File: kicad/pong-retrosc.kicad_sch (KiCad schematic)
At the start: 26 parts, among them J1 RCA video (painel), J10 PAM8403 OUT L (painel), J2 PAM8403 IN, J3 PAM8403 5V, J4 chave A/B (linha), J5 pot P1 (painel), J6 pot P2 (painel), J7 START (painel), J8 RCA audio L (painel), J9 RCA audio R (painel), SW1 START, SW2 A/B, U1 RaspberryPi_Pico

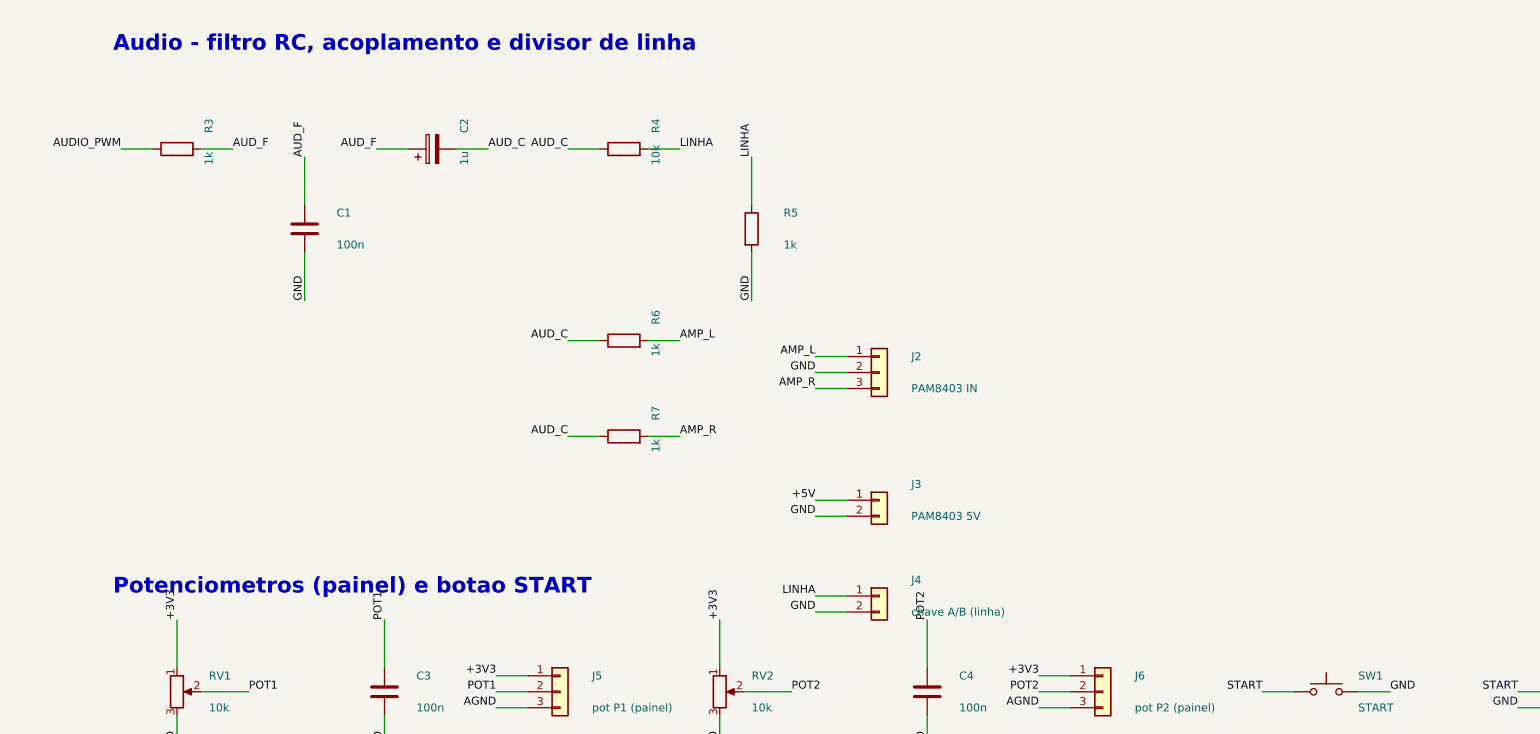
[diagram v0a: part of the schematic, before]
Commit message: kicad: sobe o ramo do amp e afasta titulo dos labels dos pots
Move R6/R7/J2/J3/J4 para a faixa do audio, a direita (antes desciam
ate U(64) e o J4 batia na linha do titulo dos potenciometros).

Sobe o titulo "Potenciometros" para U(58): os labels +3V3/POT1/POT2
sobem dos pots e alcancavam ~U(65), colidindo com o texto.

ERC continua com 0 violacoes; SVG e PDF regerados.

Co-Authored-By: Claude Opus 4.7 <noreply@anthropic.com>
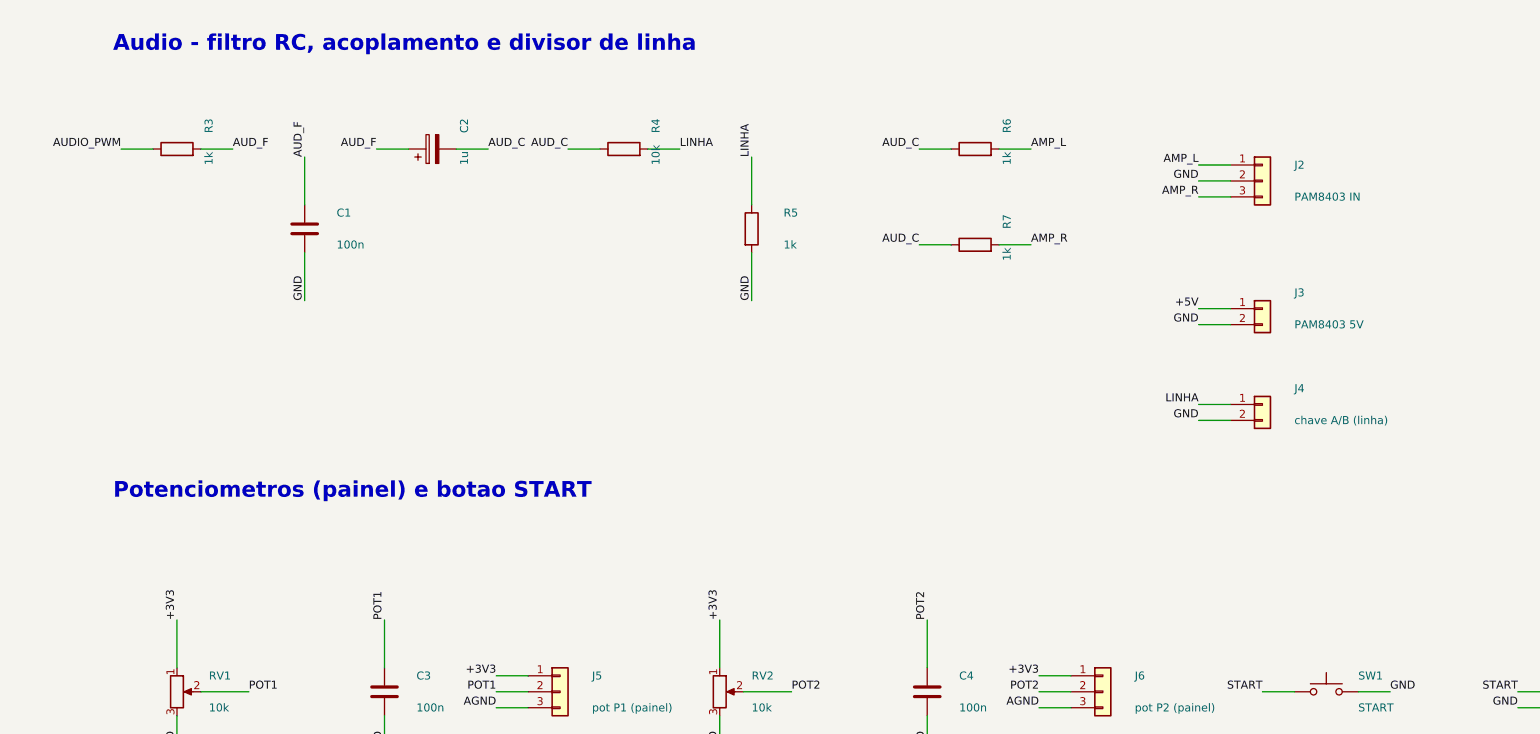
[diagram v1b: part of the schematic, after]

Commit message: kicad: esquematico refeito para a arquitetura do prototipo
As fotos do prototipo mostram RCAs e o modulo PAM8403 soldados NA
PLACA -- o esquematico tratava os dois como pecas de painel. Corrige:

- J1/J8/J9 (RCAs de video e audio) e U2 (PAM8403 HW-012) passam a ser
  on-board, com footprint.
- Substitui os headers J2/J3 (entradas/5V do amp) pelo proprio modulo
  U2, com Rout+/Rout- em No-Connect (audio e mono).
- A chave A/B fica no painel e chega por J4, agora header de 6 vias
  (RCA_C, RCA_S, LINHA, GND, LOUT_P, LOUT_N). Remove J10.
- Off-board seguem apenas: pots (J5/J6), START (J7) e a chave (J4).

Novo tools/gen_kicad_fp.py cria os dois footprints que nao existem nas
libs do KiCad (jack RCA e modulo PAM8403); validados com
"kicad-cli fp export svg". Registra a lib do projeto em fp-lib-table.

ATENCAO: as medidas desses dois footprints ainda sao PROVISORIAS --
estao marcadas com [MEDIR] no gerador e precisam ser conferidas contra
as pecas reais antes de fabricar.

ERC continua em 0 violacoes.

Co-Authored-By: Claude Opus 4.7 <noreply@anthropic.com>
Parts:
- removed J10: PAM8403 OUT L (painel), symbol Connector_Generic:Conn_01x02
- removed J2: PAM8403 IN, Connector_PinHeader_2.54mm:PinHeader_1x03_P2.54mm_Vertical, symbol Connector_Generic:Conn_01x03
- removed J3: PAM8403 5V, Connector_PinHeader_2.54mm:PinHeader_1x02_P2.54mm_Vertical, symbol Connector_Generic:Conn_01x02
- removed J4: chave A/B (linha), Connector_PinHeader_2.54mm:PinHeader_1x02_P2.54mm_Vertical, symbol Connector_Generic:Conn_01x02
- added J4: chave A/B (painel), Connector_PinHeader_2.54mm:PinHeader_1x06_P2.54mm_Vertical, symbol Connector_Generic:Conn_01x06
- added U2: PAM8403 HW-012, pong-retrosc:PAM8403_HW-012, symbol Connector_Generic:Conn_01x08
- J1: value RCA video (painel) -> RCA video (na placa); footprint Connector_PinHeader_2.54mm:PinHeader_1x02_P2.54mm_Vertical -> pong-retrosc:RCA_Jack_THT_Panel
- J8: value RCA audio L (painel) -> RCA audio L (na placa); footprint (none) -> pong-retrosc:RCA_Jack_THT_Panel
- J9: value RCA audio R (painel) -> RCA audio R (na placa); footprint (none) -> pong-retrosc:RCA_Jack_THT_Panel
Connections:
- net +5V: now also U2.1 (Pin_1)
- net AMP_L: now also U2.3 (Pin_3)
- net AMP_R: now also U2.4 (Pin_4)
- net GND: now also J4.4 (Pin_4), U2.2 (Pin_2)
- net LINHA: now also J4.3 (Pin_3)
- net LOUT_N: now also J4.6 (Pin_6), U2.6 (Pin_6)
- net LOUT_P: now also J4.5 (Pin_5), U2.5 (Pin_5)
- net RCA_C: now also J4.1 (Pin_1)
- net RCA_S: now also J4.2 (Pin_2)
- no-connect marks 24 -> 26
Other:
- note added: "Chave A/B (painel, via J4) e RCAs de audio (na placa)"
- note removed: "Chave A/B e RCAs de audio - PAINEL (fora da placa)"

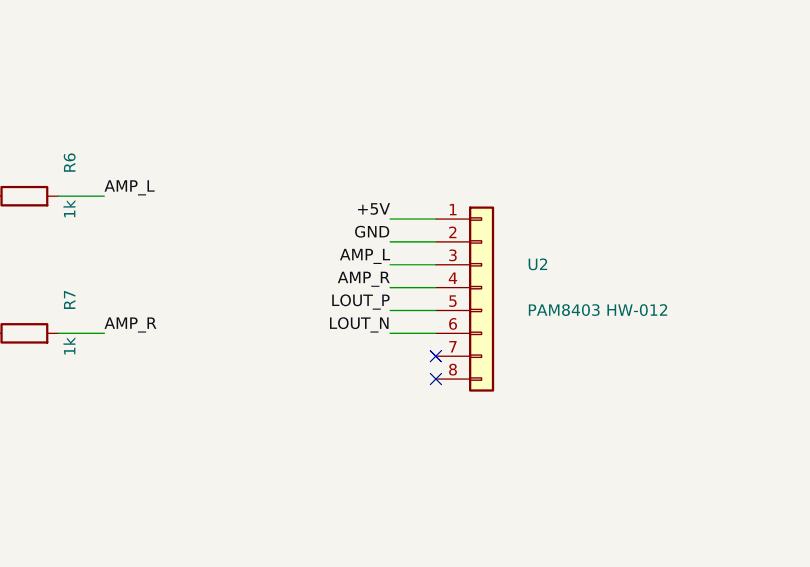
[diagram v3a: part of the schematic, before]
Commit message: kicad: PCB roteado (2 camadas, plano de GND, DRC 0 erros)
Placa gerada e roteada por scripts, reproduzivel:
- tools/gen_kicad_pcb.py: placement (audio a esquerda, video a direita
  com retornos separados; Pico no meio; headers de painel na frente),
  contorno 100x60, furos M3, zonas GND nas 2 faces e regras JLCPCB.
- tools/make_decoy.py: placa-isca sem zonas + contorno recuado 0.35mm,
  para o Freerouting rotear nas 2 camadas (com zonas ele vira quase
  mono-camada e abandona nets longos -- licao da skill kicad-freerouting).
- tools/import_ses.py: importa o SES e remove as trilhas de GND (o plano
  cuida do GND via thermal), eliminando o starved_thermal.

Freerouting roteou os 36 nets; DRC final (--refill-zones) com 0 erros
eletricos (0 unconnected/clearance/shorting/edge). Restam so avisos de
silk (cosmeticos).

Corrige a pinagem do U2 (Conn_01x09 na ordem fisica do HW-012) e ajusta
os footprints do RCA (medidas reais: sinal + 3 abas de terra a 5mm,
furos oblongos) e do PAM8403 (montagem vertical/SIP).

Inclui gerbers + furacao em kicad/gerbers/ e kicad/README.md com o
pipeline completo. Remove tools/post_route.py (obsoleto: era o
roteamento manual dos 2 nets que a isca resolveu).

Co-Authored-By: Claude Opus 4.7 <noreply@anthropic.com>
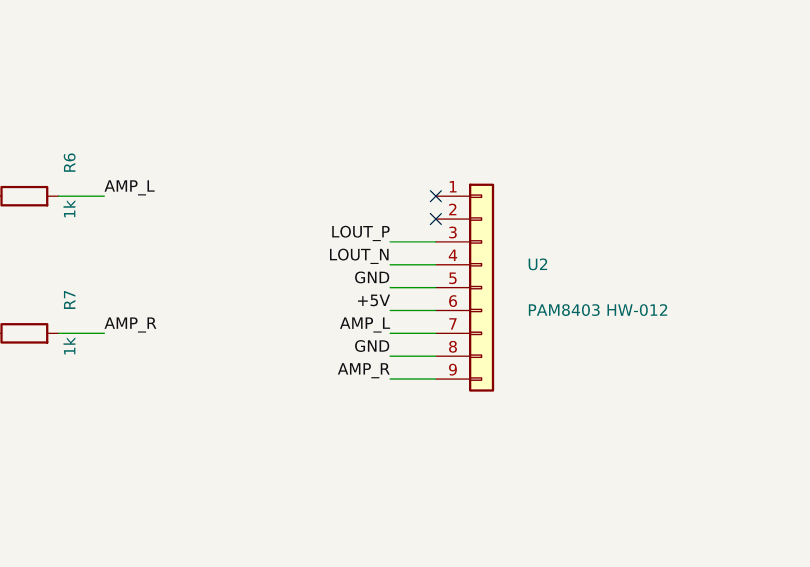
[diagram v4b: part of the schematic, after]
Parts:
- removed U2: PAM8403 HW-012, pong-retrosc:PAM8403_HW-012, symbol Connector_Generic:Conn_01x08
- added U2: PAM8403 HW-012, pong-retrosc:PAM8403_HW-012, symbol Connector_Generic:Conn_01x09
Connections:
- net +5V: now also U2.6 (Pin_6)
- net AMP_L: now also U2.7 (Pin_7)
- net AMP_R: now also U2.9 (Pin_9)
- net GND: now also U2.5 (Pin_5), U2.8 (Pin_8)
- net LOUT_N: now also U2.4 (Pin_4)
- net LOUT_P: now also U2.3 (Pin_3)
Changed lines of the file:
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@@
 		(instances
 			(project "pong-retrosc"
-				(path "/96b8633d-64ce-4605-8e3d-9ed899d2ea24"
+				(path "/54382c2c-30b3-43b0-8332-7c9095b4b1c1"
 					(reference "U1")
 					(unit 1)
@@
 		(instances
 			(project "pong-retrosc"
-				(path "/96b8633d-64ce-4605-8e3d-9ed899d2ea24"
+				(path "/54382c2c-30b3-43b0-8332-7c9095b4b1c1"
 					(reference "R1")
 					(unit 1)
@@
 		(instances
 			(project "pong-retrosc"
-				(path "/96b8633d-64ce-4605-8e3d-9ed899d2ea24"
+				(path "/54382c2c-30b3-43b0-8332-7c9095b4b1c1"
 					(reference "R2")
 					(unit 1)
@@
 		(instances
 			(project "pong-retrosc"
-				(path "/96b8633d-64ce-4605-8e3d-9ed899d2ea24"
+				(path "/54382c2c-30b3-43b0-8332-7c9095b4b1c1"
 					(reference "J1")
 					(unit 1)
@@
 		(instances
 			(project "pong-retrosc"
-				(path "/96b8633d-64ce-4605-8e3d-9ed899d2ea24"
+				(path "/54382c2c-30b3-43b0-8332-7c9095b4b1c1"
 					(reference "R3")
 					(unit 1)
@@
 		(instances
 			(project "pong-retrosc"
-				(path "/96b8633d-64ce-4605-8e3d-9ed899d2ea24"
+				(path "/54382c2c-30b3-43b0-8332-7c9095b4b1c1"
 					(reference "C1")
 					(unit 1)
@@
 		(instances
 			(project "pong-retrosc"
-				(path "/96b8633d-64ce-4605-8e3d-9ed899d2ea24"
+				(path "/54382c2c-30b3-43b0-8332-7c9095b4b1c1"
 					(reference "C2")
 					(unit 1)
@@
 		(instances
 			(project "pong-retrosc"
-				(path "/96b8633d-64ce-4605-8e3d-9ed899d2ea24"
+				(path "/54382c2c-30b3-43b0-8332-7c9095b4b1c1"
 					(reference "R4")
 					(unit 1)
@@
 		(instances
 			(project "pong-retrosc"
-				(path "/96b8633d-64ce-4605-8e3d-9ed899d2ea24"
+				(path "/54382c2c-30b3-43b0-8332-7c9095b4b1c1"
 					(reference "R5")
 					(unit 1)
@@
 		(instances
 			(project "pong-retrosc"
-				(path "/96b8633d-64ce-4605-8e3d-9ed899d2ea24"
+				(path "/54382c2c-30b3-43b0-8332-7c9095b4b1c1"
 					(reference "R6")
 					(unit 1)
@@
 		(instances
 			(project "pong-retrosc"
-				(path "/96b8633d-64ce-4605-8e3d-9ed899d2ea24"
+				(path "/54382c2c-30b3-43b0-8332-7c9095b4b1c1"
 					(reference "R7")
 					(unit 1)
@@
 	)
 	(symbol
-		(lib_id "Connector_Generic:Conn_01x08")
+		(lib_id "Connector_Generic:Conn_01x09")
 		(at 309.88 101.6 0)
 		(unit 1)
@@
 		(pin "7")
 		(pin "8")
+		(pin "9")
 		(instances
 			(project "pong-retrosc"
-				(path "/96b8633d-64ce-4605-8e3d-9ed899d2ea24"
+				(path "/54382c2c-30b3-43b0-8332-7c9095b4b1c1"
 					(reference "U2")
 					(unit 1)
@@
 	(wire
 		(pts
-			(xy 304.8 93.98) (xy 299.72 93.98)
+			(xy 304.8 96.52) (xy 299.72 96.52)
 		)
 		(stroke
@@
 		)
 	)
-	(label "+5V"
-		(at 299.72 93.98 0)
+	(label "LOUT_P"
+		(at 299.72 96.52 0)
 		(effects
 			(font
@@
 	(wire
 		(pts
-			(xy 304.8 96.52) (xy 299.72 96.52)
+			(xy 304.8 99.06) (xy 299.72 99.06)
+		)
+		(stroke
+			(width 0)
+			(type default)
+		)
+	)
+	(label "LOUT_N"
+		(at 299.72 99.06 0)
+		(effects
+			(font
+				(size 1.27 1.27)
+			)
+			(justify right bottom)
+		)
+	)
+	(wire
+		(pts
+			(xy 304.8 101.6) (xy 299.72 101.6)
 		)
 		(stroke
@@
 	)
 	(label "GND"
-		(at 299.72 96.52 0)
+		(at 299.72 101.6 0)
 		(effects
 			(font
@@
 	(wire
 		(pts
-			(xy 304.8 99.06) (xy 299.72 99.06)
+			(xy 304.8 104.14) (xy 299.72 104.14)
 		)
 		(stroke
@@
 		)
 	)
-	(label "AMP_L"
-		(at 299.72 99.06 0)
+	(label "+5V"
+		(at 299.72 104.14 0)
 		(effects
 			(font
@@
 	(wire
 		(pts
-			(xy 304.8 101.6) (xy 299.72 101.6)
+			(xy 304.8 106.68) (xy 299.72 106.68)
 		)
 		(stroke
@@
 		)
 	)
-	(label "AMP_R"
-		(at 299.72 101.6 0)
+	(label "AMP_L"
+		(at 299.72 106.68 0)
 		(effects
 			(font
@@
 	(wire
 		(pts
-			(xy 304.8 104.14) (xy 299.72 104.14)
+			(xy 304.8 109.22) (xy 299.72 109.22)
 		)
 		(stroke
@@
 		)
 	)
-	(label "LOUT_P"
-		(at 299.72 104.14 0)
+	(label "GND"
+		(at 299.72 109.22 0)
 		(effects
 			(font
@@
 	(wire
 		(pts
-			(xy 304.8 106.68) (xy 299.72 106.68)
+			(xy 304.8 111.76) (xy 299.72 111.76)
 		)
 		(stroke
@@
 		)
 	)
-	(label "LOUT_N"
-		(at 299.72 106.68 0)
+	(label "AMP_R"
+		(at 299.72 111.76 0)
 		(effects
 			(font
@@
 	)
 	(no_connect
-		(at 304.8 109.22)
+		(at 304.8 91.44)
 	)
 	(no_connect
-		(at 304.8 111.76)
+		(at 304.8 93.98)
 	)
 	(text "Potenciometros (painel) e botao START"
@@
 		(instances
 			(project "pong-retrosc"
-				(path "/96b8633d-64ce-4605-8e3d-9ed899d2ea24"
+				(path "/54382c2c-30b3-43b0-8332-7c9095b4b1c1"
 					(reference "RV1")
 					(unit 1)
@@
 		(instances
 			(project "pong-retrosc"
-				(path "/96b8633d-64ce-4605-8e3d-9ed899d2ea24"
+				(path "/54382c2c-30b3-43b0-8332-7c9095b4b1c1"
 					(reference "C3")
 					(unit 1)
@@
 		(instances
 			(project "pong-retrosc"
-				(path "/96b8633d-64ce-4605-8e3d-9ed899d2ea24"
+				(path "/54382c2c-30b3-43b0-8332-7c9095b4b1c1"
 					(reference "J5")
 					(unit 1)
@@
 		(instances
 			(project "pong-retrosc"
-				(path "/96b8633d-64ce-4605-8e3d-9ed899d2ea24"
+				(path "/54382c2c-30b3-43b0-8332-7c9095b4b1c1"
 					(reference "RV2")
 					(unit 1)
@@
 		(instances
 			(project "pong-retrosc"
-				(path "/96b8633d-64ce-4605-8e3d-9ed899d2ea24"
+				(path "/54382c2c-30b3-43b0-8332-7c9095b4b1c1"
 					(reference "C4")
 					(unit 1)
@@
 		(instances
 			(project "pong-retrosc"
-				(path "/96b8633d-64ce-4605-8e3d-9ed899d2ea24"
+				(path "/54382c2c-30b3-43b0-8332-7c9095b4b1c1"
 					(reference "J6")
 					(unit 1)
@@
 		(instances
 			(project "pong-retrosc"
-				(path "/96b8633d-64ce-4605-8e3d-9ed899d2ea24"
+				(path "/54382c2c-30b3-43b0-8332-7c9095b4b1c1"
 					(reference "SW1")
 					(unit 1)
@@
 		(instances
 			(project "pong-retrosc"
-				(path "/96b8633d-64ce-4605-8e3d-9ed899d2ea24"
+				(path "/54382c2c-30b3-43b0-8332-7c9095b4b1c1"
 					(reference "J7")
 					(unit 1)
@@
 		(instances
 			(project "pong-retrosc"
-				(path "/96b8633d-64ce-4605-8e3d-9ed899d2ea24"
+				(path "/54382c2c-30b3-43b0-8332-7c9095b4b1c1"
 					(reference "J4")
 					(unit 1)
@@
 		(instances
 			(project "pong-retrosc"
-				(path "/96b8633d-64ce-4605-8e3d-9ed899d2ea24"
+				(path "/54382c2c-30b3-43b0-8332-7c9095b4b1c1"
 					(reference "SW2")
 					(unit 1)
@@
 		(instances
 			(project "pong-retrosc"
-				(path "/96b8633d-64ce-4605-8e3d-9ed899d2ea24"
+				(path "/54382c2c-30b3-43b0-8332-7c9095b4b1c1"
 					(reference "SW2")
 					(unit 2)
@@
 		(instances
 			(project "pong-retrosc"
-				(path "/96b8633d-64ce-4605-8e3d-9ed899d2ea24"
+				(path "/54382c2c-30b3-43b0-8332-7c9095b4b1c1"
 					(reference "J8")
 					(unit 1)
@@
 		(instances
 			(project "pong-retrosc"
-				(path "/96b8633d-64ce-4605-8e3d-9ed899d2ea24"
+				(path "/54382c2c-30b3-43b0-8332-7c9095b4b1c1"
 					(reference "J9")
 					(unit 1)
